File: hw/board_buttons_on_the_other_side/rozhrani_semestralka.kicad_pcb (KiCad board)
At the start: 2 copper layers, 152 x 38.6 mm, 65 parts, among them P1 DISPLAY_CONN, P2 DISPLAY_VCC_CON, P3 USB_B, Q1 BC847, U1 MCP2210, U2 MIC5504, U3 Joystick, U4 LM239, U5 CD4532, U6 NPIC6C596, U7 NE555, U8 PB6149L, U9 PB6149Ldual

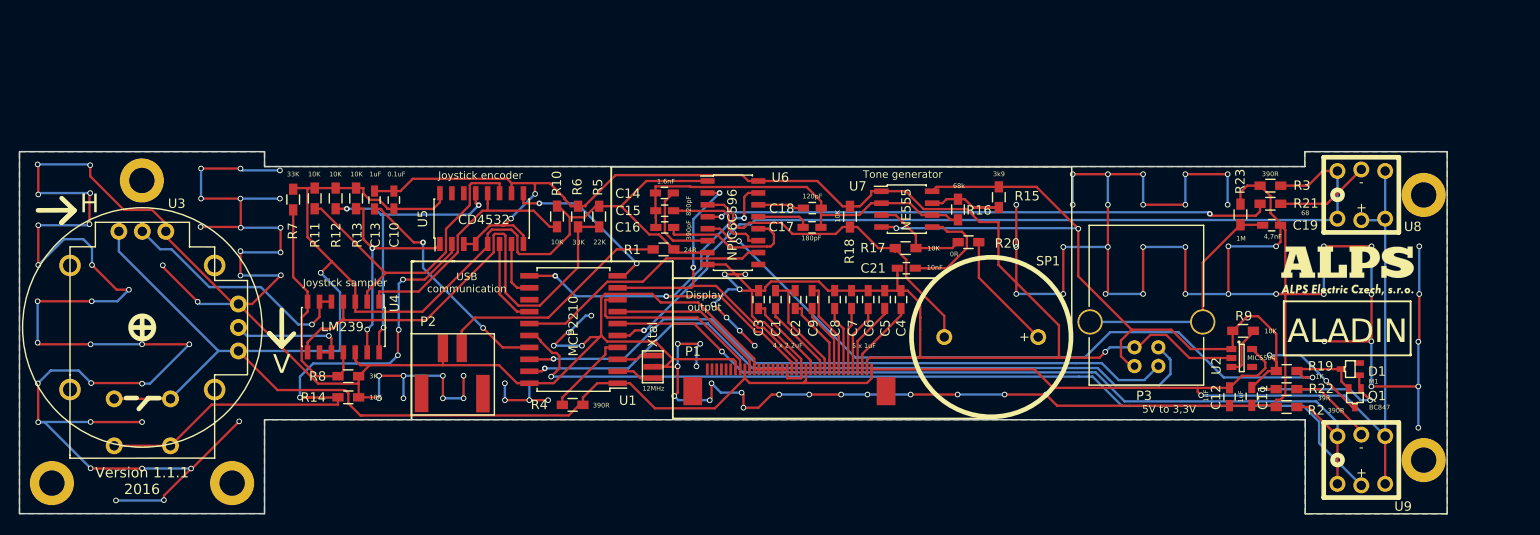
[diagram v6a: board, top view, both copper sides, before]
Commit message: Aladin v 1.2.0 pcb - repaired GPIO for /CE and also BUZZERs capacitors, some footprints had change
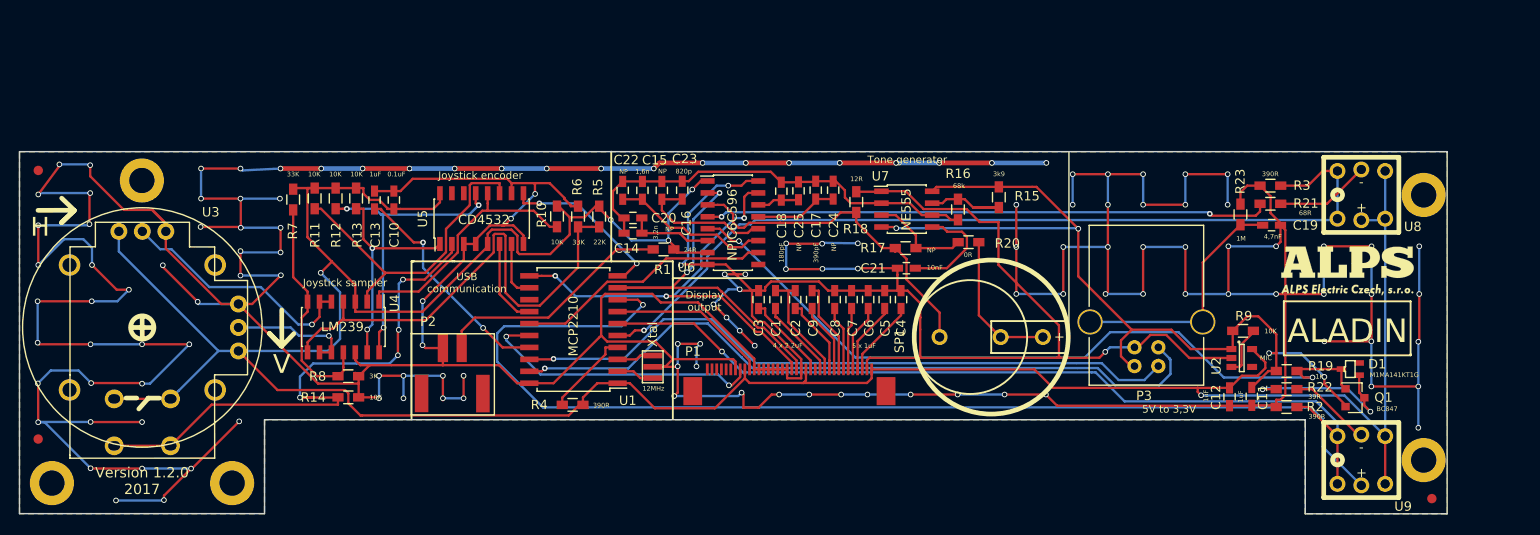
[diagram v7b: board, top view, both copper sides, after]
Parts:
- added C20: NP, Capacitors_SMD:C_0603_HandSoldering, F.Cu at (132.2, 103.7)
- added C22: NP, Capacitors_SMD:C_0603_HandSoldering, F.Cu at (131.1, 100.7)
- added C23: NP, Capacitors_SMD:C_0603_HandSoldering, F.Cu at (135.3, 100.7)
- added C24: NP, Capacitors_SMD:C_0603_HandSoldering, F.Cu at (153.5, 100.7)
- added C25: NP, Capacitors_SMD:C_0603_HandSoldering, F.Cu at (149.8, 100.8)
- added FID1: Fiducial_1mm_Dia_2.54mm_Outer_CopperTop, Fiducials:Fiducial_1mm_Dia_2.54mm_Outer_CopperTop, F.Cu at (68.9, 98.6)
- added FID2: Fiducial_1mm_Dia_2.54mm_Outer_CopperTop, Fiducials:Fiducial_1mm_Dia_2.54mm_Outer_CopperTop, F.Cu at (68.9, 127.2)
- added FID3**: Fiducial_1mm_Dia_2.54mm_Outer_CopperTop, Fiducials:Fiducial_1mm_Dia_2.54mm_Outer_CopperTop, F.Cu at (217.2, 133.5)
- C14: value 1.6nF -> 3,2n
- C15: value 820pF -> 1,6n
- C16: value 390pF -> 820p
- C17: value 180pF -> 390pF
- C18: value 120pF -> 180pF
- D1: value M1 -> M1MA141KT1G
- Q1: footprint TO_SOT_Packages_SMD:SOT-323 -> TO_SOT_Packages_SMD:SOT-23
- R17: value 10K -> NP
- R18: value 10K -> 12R
- R21: value 68 -> 68R
- U2: value MIC5504 -> MIC
- moved C14 5.43 mm to (132.2, 105.3)
- moved C16 4.38 mm to (137.4, 100.7), turned to 270 degrees
- moved C17 3.98 mm to (151.6, 100.7), turned to 270 degrees
- moved C18 3.76 mm to (148.0, 100.8), turned to 270 degrees
- moved C15 3.21 mm to (133.2, 100.7), turned to 270 degrees
- moved R18 1.69 mm to (156.0, 102.0)
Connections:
- D1 pad 2: (no net) -> Net-(D1-Pad2)
- P1 pad 13: (no net) -> Net-(P1-Pad13)
- P1 pad 31: (no net) -> Net-(P1-Pad31)
- P1 pad 32: (no net) -> Net-(P1-Pad32)
- P1 pad 33: (no net) -> Net-(P1-Pad33)
- P1 pad 34: (no net) -> Net-(P1-Pad34)
- P1 pad 35: (no net) -> Net-(P1-Pad35)
- P1 pad 36: (no net) -> Net-(P1-Pad36)
- Q1 pad 1: /BUT_LED -> /REG2
- Q1 pad 2: /REG2 -> VCC
- Q1 pad 3: VCC -> /BUT_LED
- U1 pad 13: (no net) -> /MISO
- U1 pad 16: /SIGNAL_LED -> //CE
- U1 pad 8: //CE -> /SIGNAL_LED
- U2 pad 4: (no net) -> Net-(U2-Pad4)
- U5 pad 14: (no net) -> Net-(U5-Pad14)
- U5 pad 15: (no net) -> Net-(U5-Pad15)
- U6 pad 9: (no net) -> Net-(U6-Pad9)
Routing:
- net GND: track 850.8 -> 944.1 mm, vias 118 -> 137
- net /SIGNAL_LED: track 99.2 -> 122.0 mm
- net //CE: track 20.3 -> 31.6 mm, vias 0 -> 2
- net (no net): track 8.20 -> 0.00 mm, vias 4 -> 0
- net /MOSI: track 35.7 -> 42.5 mm
- net /REG4: track 11.4 -> 16.9 mm
- net Net-(C14-Pad1): track 42.0 -> 45.4 mm
- net /REG6: track 5.65 -> 8.90 mm
- net Net-(R20-Pad2): track 12.7 -> 15.6 mm
- net +3V3: track 334.0 -> 331.8 mm, vias 2 -> 5
- net /BUT_LED: track 16.5 -> 18.4 mm
- net VCC: track 97.5 -> 95.7 mm
- net /REG0: track 35.8 -> 36.6 mm
- net /REG3: track 9.49 -> 8.94 mm
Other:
- outline, holes or cut-outs redrawn
- board text added: "Version 1.2.0 2017"
- board text removed: "Version 1.1.1 2016"
